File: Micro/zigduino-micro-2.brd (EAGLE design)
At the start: 20.3 x 48.3 mm, 49 parts, among them J2 USB-MINI-B, Q1 AMB8G, Q2 ABS10, Q3 BSS84, U1 ATMEGA1284RFR2, U2 USD-SOCKETNEW, U3 MCP73831, U4 MCP1804-5002I/OT, U5 MCP1804-3302I/OT

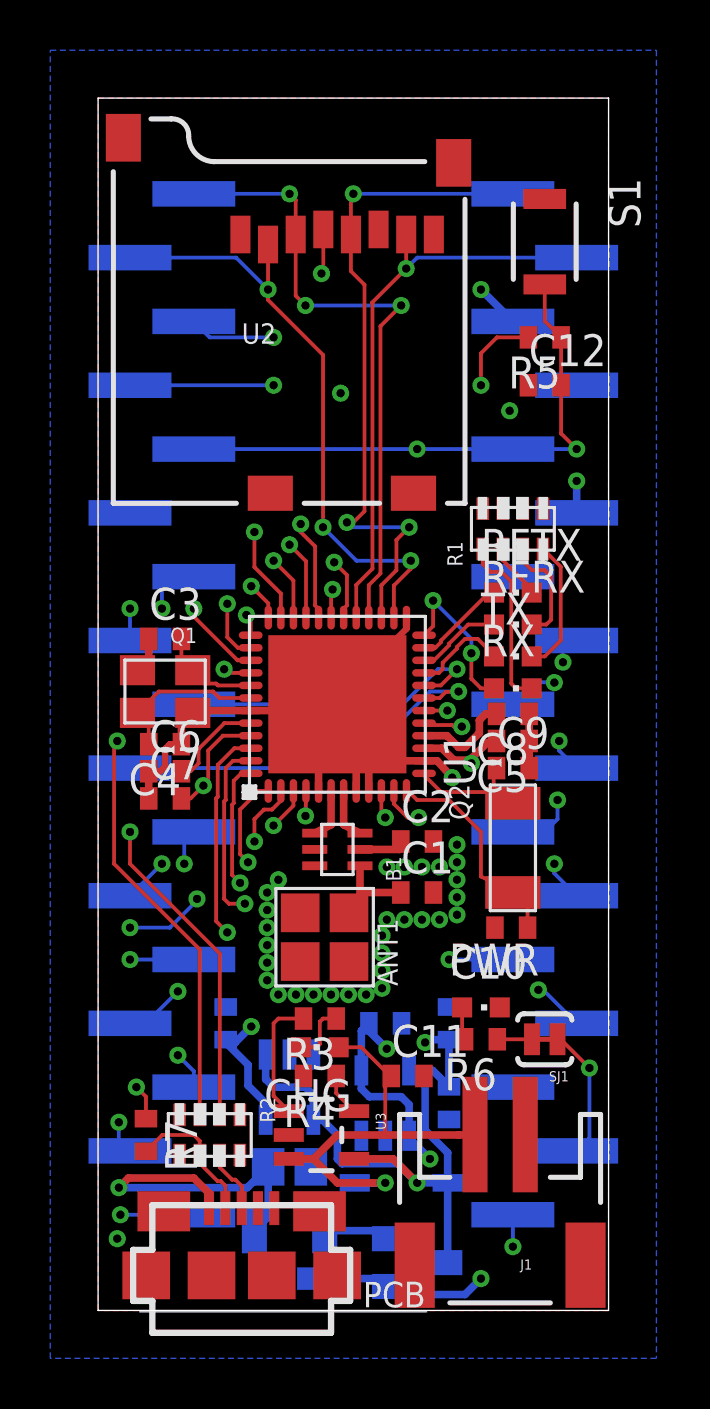
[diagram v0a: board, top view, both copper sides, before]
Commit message: added Zigduino Micro files updated burning instructions added Zigduino r3 files
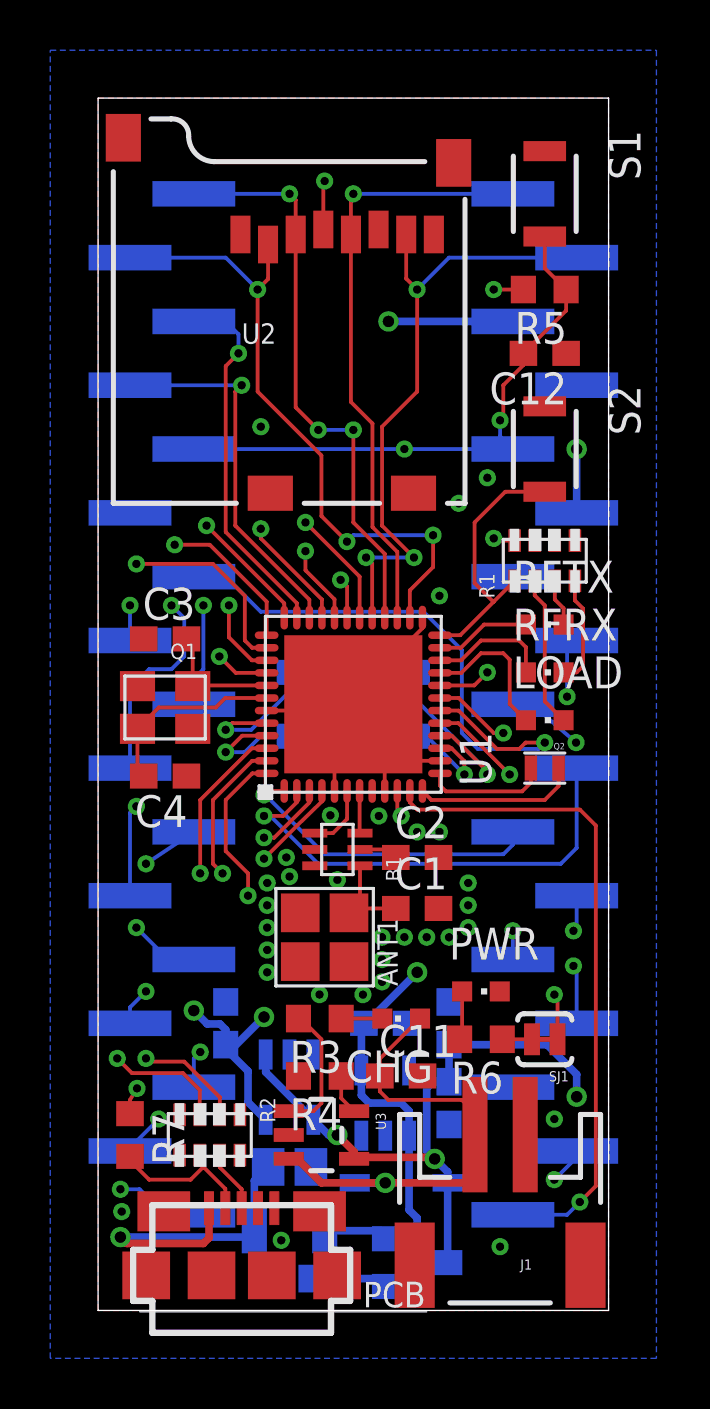
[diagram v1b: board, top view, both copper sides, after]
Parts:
- removed C10, C9: (no value), resistor:C0402
- removed RX, TX: AMB, led:CHIPLED_0603
- added LOAD: RED, led:CHIPLED_0603
- added S2: B3U-1000, logos-faves:B3U
- C1, C11, C12, C14, C15, C16, C17, C2, C3, C4, C5, C6, C7, C8: device resistor:C0402 -> resistor:C0603
- Q2: value ABS10 -> ABS05; device logos-crystals:ABS10 -> logos-crystals:ABS05
- R3, R4, R5, R6, R7, R8: device resistor:R0402 -> resistor:R0603
- moved C7 9.47 mm to (11.8, 22.9), flipped to the bottom, turned to 180 degrees
- moved C5 8.00 mm to (8.51, 22.9), flipped to the bottom, turned to 0 degrees
- moved C6 7.04 mm to (8.51, 25.4), flipped to the bottom
- moved C8 4.98 mm to (11.8, 25.4), flipped to the bottom
- moved CHG 3.43 mm to (12.1, 11.6)
- moved Q2 3.42 mm to (17.8, 21.6), turned to 0 degrees
- moved RFRX 2.29 mm to (17.8, 25.4)
- moved R5 1.91 mm to (17.8, 40.6)
- moved S1 1.91 mm to (17.8, 44.5)
- moved R1 1.80 mm to (17.8, 29.8)
- moved RFTX 1.80 mm to (17.8, 27.3)
- moved C12 1.27 mm to (17.8, 38.1), turned to 180 degrees
- moved C4 1.27 mm to (2.67, 21.3)
- moved C1 0.64 mm to (12.7, 16.0)
- moved C2 0.64 mm to (12.7, 18.0)
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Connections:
- removed net N$24: R1.7, TX.C
- net +3V3: now also R1.2
- net GND: now also S2.1; no longer C10.2, C9.2, R1.2
- net N$11: now also LOAD.A, U1.21; no longer RX.A, U1.24
- net N$17: now also R1.7; no longer R1.5
- net N$18: now also R1.5; no longer R1.3
- net N$21: now also LOAD.C, R1.3; no longer R1.1, RX.C
- net N$22: now also R1.1, S2.2, U1.24; no longer TX.A, U1.21
- net N$6: no longer C10.1
- net N$9: no longer C9.1
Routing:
- net D5/RX1: track 15.8 -> 38.8 mm, vias 1 -> 3
- net D3/SCL: track 18.0 -> 34.8 mm
- net GND: track 36.0 -> 19.9 mm, vias 34 -> 30
- net D6: track 14.4 -> 25.6 mm
- net D7: track 16.6 -> 26.9 mm
- net A2: track 20.7 -> 29.0 mm
- net A3: track 19.8 -> 12.4 mm, vias 2 -> 1
- net D2/SDA: track 16.8 -> 23.8 mm, vias 2 -> 1
- net A5: track 18.2 -> 25.1 mm
- net N$22: track 3.85 -> 10.6 mm
- net D4/TX1: track 12.6 -> 19.3 mm, vias 1 -> 2
- net N$13: track 28.7 -> 34.6 mm
- net N$24: track 5.36 -> 0.00 mm
- net VIN: track 62.5 -> 57.3 mm, vias 4 -> 2
- net A0: track 26.6 -> 31.5 mm
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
